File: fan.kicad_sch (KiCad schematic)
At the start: 15 parts, among them J5001 Conn_01x04, U5001 EMC2103-2

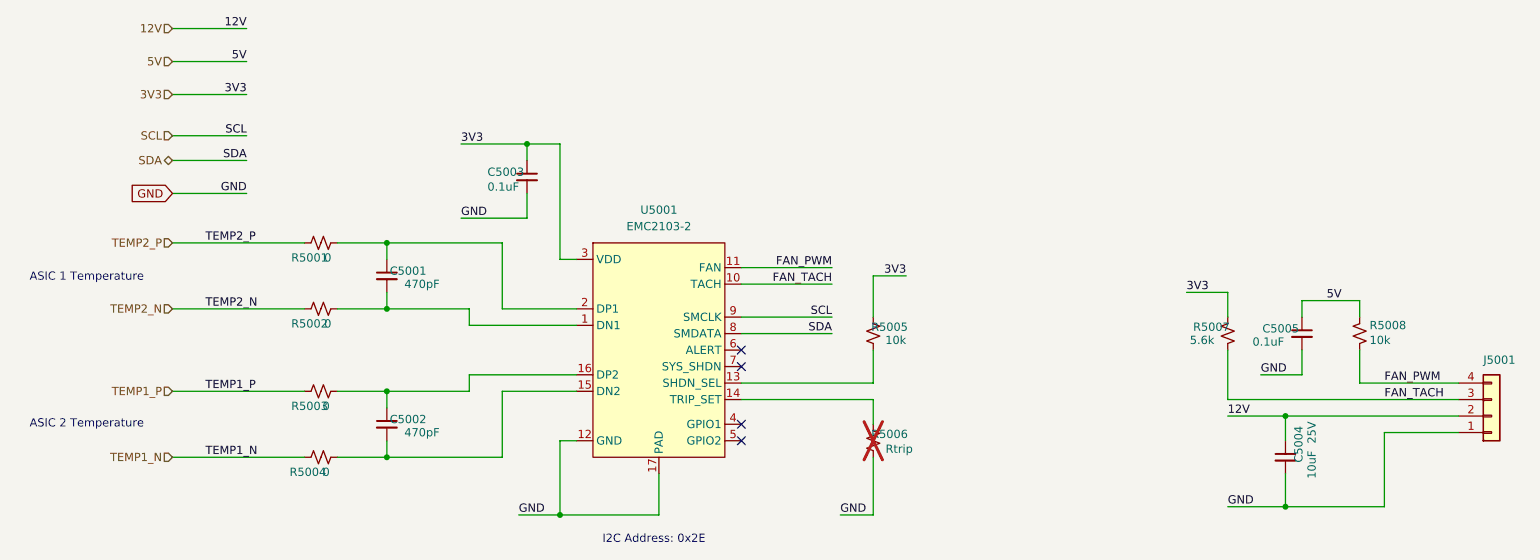
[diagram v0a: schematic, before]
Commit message: finished adding ASICs to schematic. Change VR to single phase 2.8V output
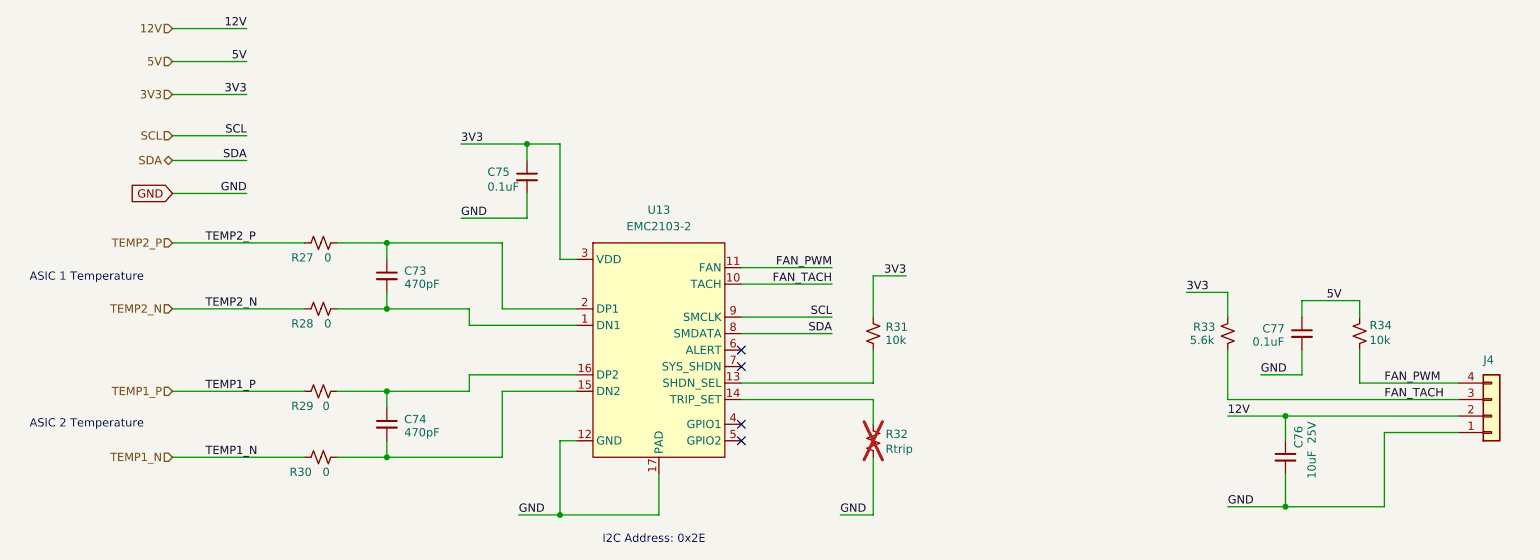
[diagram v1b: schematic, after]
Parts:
- renumbered C5001 to C73, C5002 to C74, C5003 to C75, C5004 to C76, C5005 to C77, J5001 to J4, R5001 to R27, R5002 to R28, R5003 to R29, R5004 to R30, R5005 to R31, R5006 to R32, R5007 to R33, R5008 to R34, U5001 to U13
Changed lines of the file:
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@@
 		(on_board yes)
 		(dnp no)
-		(property "Reference" "R5003"
+		(property "Reference" "R29"
 			(at 75.438 105.156 90)
 			(effects
@@
 			(project "BitaxeGT"
 				(path "/61fe8d2c-9301-4ad9-8caf-c47acfa835b0/edab3562-ad75-4c4e-afab-a1841dcf5714"
-					(reference "R5003")
+					(reference "R29")
 					(unit 1)
 				)
@@
 		(on_board yes)
 		(dnp yes)
-		(property "Reference" "R5006"
+		(property "Reference" "R32"
 			(at 170.434 109.474 0)
 			(effects
@@
 			(project "BitaxeGT"
 				(path "/61fe8d2c-9301-4ad9-8caf-c47acfa835b0/edab3562-ad75-4c4e-afab-a1841dcf5714"
-					(reference "R5006")
+					(reference "R32")
 					(unit 1)
 				)
@@
 		(dnp no)
 		(fields_autoplaced yes)
-		(property "Reference" "U5001"
+		(property "Reference" "U13"
 			(at 132.08 74.93 0)
 			(effects
@@
 			(project ""
 				(path "/61fe8d2c-9301-4ad9-8caf-c47acfa835b0/edab3562-ad75-4c4e-afab-a1841dcf5714"
-					(reference "U5001")
+					(reference "U13")
 					(unit 1)
 				)
@@
 		(on_board yes)
 		(dnp no)
-		(property "Reference" "C5001"
+		(property "Reference" "C73"
 			(at 96.266 84.328 0)
 			(effects
@@
 			(project "BitaxeGT"
 				(path "/61fe8d2c-9301-4ad9-8caf-c47acfa835b0/edab3562-ad75-4c4e-afab-a1841dcf5714"
-					(reference "C5001")
+					(reference "C73")
 					(unit 1)
 				)
@@
 		(on_board yes)
 		(dnp no)
-		(property "Reference" "R5005"
+		(property "Reference" "R31"
 			(at 170.434 92.964 0)
 			(effects
@@
 			(project "BitaxeGT"
 				(path "/61fe8d2c-9301-4ad9-8caf-c47acfa835b0/edab3562-ad75-4c4e-afab-a1841dcf5714"
-					(reference "R5005")
+					(reference "R31")
 					(unit 1)
 				)
@@
 		(on_board yes)
 		(dnp no)
-		(property "Reference" "R5008"
+		(property "Reference" "R34"
 			(at 241.554 92.71 0)
 			(effects
@@
 			(project "BitaxeGT"
 				(path "/61fe8d2c-9301-4ad9-8caf-c47acfa835b0/edab3562-ad75-4c4e-afab-a1841dcf5714"
-					(reference "R5008")
+					(reference "R34")
 					(unit 1)
 				)
@@
 		(on_board yes)
 		(dnp no)
-		(property "Reference" "C5002"
+		(property "Reference" "C74"
 			(at 96.266 107.188 0)
 			(effects
@@
 			(project "BitaxeGT"
 				(path "/61fe8d2c-9301-4ad9-8caf-c47acfa835b0/edab3562-ad75-4c4e-afab-a1841dcf5714"
-					(reference "C5002")
+					(reference "C74")
 					(unit 1)
 				)
@@
 		(on_board yes)
 		(dnp no)
-		(property "Reference" "J5001"
+		(property "Reference" "J4"
 			(at 259.08 98.044 0)
 			(effects
@@
 			(project "BitaxeGT"
 				(path "/61fe8d2c-9301-4ad9-8caf-c47acfa835b0/edab3562-ad75-4c4e-afab-a1841dcf5714"
-					(reference "J5001")
+					(reference "J4")
 					(unit 1)
 				)
@@
 		(on_board yes)
 		(dnp no)
-		(property "Reference" "R5004"
+		(property "Reference" "R30"
 			(at 75.184 115.316 90)
 			(effects
@@
 			(project "BitaxeGT"
 				(path "/61fe8d2c-9301-4ad9-8caf-c47acfa835b0/edab3562-ad75-4c4e-afab-a1841dcf5714"
-					(reference "R5004")
+					(reference "R30")
 					(unit 1)
 				)
@@
 		(on_board yes)
 		(dnp no)
-		(property "Reference" "R5007"
+		(property "Reference" "R33"
 			(at 214.376 92.964 0)
 			(effects
@@
 			(project "BitaxeGT"
 				(path "/61fe8d2c-9301-4ad9-8caf-c47acfa835b0/edab3562-ad75-4c4e-afab-a1841dcf5714"
-					(reference "R5007")
+					(reference "R33")
 					(unit 1)
 				)
@@
 		(on_board yes)
 		(dnp no)
-		(property "Reference" "C5003"
+		(property "Reference" "C75"
 			(at 105.664 69.088 0)
 			(effects
@@
 			(project "BitaxeGT"
 				(path "/61fe8d2c-9301-4ad9-8caf-c47acfa835b0/edab3562-ad75-4c4e-afab-a1841dcf5714"
-					(reference "C5003")
+					(reference "C75")
 					(unit 1)
 				)
@@
 		(on_board yes)
 		(dnp no)
-		(property "Reference" "C5005"
+		(property "Reference" "C77"
 			(at 225.044 93.218 0)
 			(effects
@@
 			(project "BitaxeGT"
 				(path "/61fe8d2c-9301-4ad9-8caf-c47acfa835b0/edab3562-ad75-4c4e-afab-a1841dcf5714"
-					(reference "C5005")
+					(reference "C77")
 					(unit 1)
 				)
@@
 		(on_board yes)
 		(dnp no)
-		(property "Reference" "R5002"
+		(property "Reference" "R28"
 			(at 75.438 92.456 90)
 			(effects
@@
 			(project "BitaxeGT"
 				(path "/61fe8d2c-9301-4ad9-8caf-c47acfa835b0/edab3562-ad75-4c4e-afab-a1841dcf5714"
-					(reference "R5002")
+					(reference "R28")
 					(unit 1)
 				)
@@
 		(on_board yes)
 		(dnp no)
-		(property "Reference" "C5004"
+		(property "Reference" "C76"
 			(at 230.632 108.204 90)
 			(effects
@@
 			(project "BitaxeGT"
 				(path "/61fe8d2c-9301-4ad9-8caf-c47acfa835b0/edab3562-ad75-4c4e-afab-a1841dcf5714"
-					(reference "C5004")
+					(reference "C76")
 					(unit 1)
 				)
@@
 		(on_board yes)
 		(dnp no)
-		(property "Reference" "R5001"
+		(property "Reference" "R27"
 			(at 75.438 82.296 90)
 			(effects
@@
 			(project "BitaxeGT"
 				(path "/61fe8d2c-9301-4ad9-8caf-c47acfa835b0/edab3562-ad75-4c4e-afab-a1841dcf5714"
-					(reference "R5001")
-					(unit 1)
-				)
+					(reference "R27")
+					(unit 1)
+				)

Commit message: Removed EMC2103, added discrete fan control, DRC pass, fixed logo.
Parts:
- removed C73, C74: 470pF, Capacitor_SMD:C_0402_1005Metric, symbol Device:C_Small
- removed C75: 0.1uF, Capacitor_SMD:C_0402_1005Metric, symbol Device:C_Small
- removed R27, R28, R29, R30: 0, Resistor_SMD:R_0402_1005Metric, symbol Device:R_Small_US
- removed R31: 10k, Resistor_SMD:R_0402_1005Metric, symbol Device:R_Small_US
- removed R32: Rtrip, Resistor_SMD:R_0402_1005Metric, symbol Device:R_Small_US
- removed U13: EMC2103-2, Package_DFN_QFN:QFN-16-1EP_4x4mm_P0.65mm_EP2.1x2.1mm, symbol bitaxe:EMC2103-2
- added D13: 3.3V Zener, Diode_SMD:D_SOD-123, symbol Device:D_Zener_Small_Filled
- added Q1: BSS138, Package_TO_SOT_SMD:SOT-23, symbol Transistor_FET:BSS138
- added R1: 1k, Resistor_SMD:R_0402_1005Metric, symbol Device:R_Small_US
- added R2: 10k, Resistor_SMD:R_0402_1005Metric, symbol Device:R_Small_US
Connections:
- net FAN_PWM: now also R1.2; no longer J4.4 (Pin_4), R34.1
- net FAN_TACH: now also R2.2; no longer J4.3 (Pin_3), R33.1
- net GND: now also D13.2 (A), Q1.2 (S)
- new net: Q1.1 (G), R1.1
- new net FAN_PWM_PIN: J4.4 (Pin_4), Q1.3 (D), R34.1
- new net FAN_TACH_PIN: D13.1 (K), J4.3 (Pin_3), R2.1, R33.1
- no-connect marks 4 -> 0
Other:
- note removed: "ASIC 1 Temperature"
- note removed: "ASIC 2 Temperature"
- note removed: "I2C Address: 0x2E"
- moved on the sheet: C76, C77, J4, R33, R34

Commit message: power plane cleanup. added field vias. generated BOM
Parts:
- R1: DK (none) -> 311-1.00KLRCT-ND; PARTNO (none) -> RC0402FR-071KL
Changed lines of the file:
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@@
 		(title "Bitaxe Intel Reference Design System")
 		(date "2025-10-01")
-		(rev "1300x")
+		(rev "1300xx")
 	)
 	(junction
@@
 			)
 		)
+		(property "Manufacturer" ""
+			(at 127 92.71 0)
+			(effects
+				(font
+					(size 1.27 1.27)
+				)
+				(hide yes)
+			)
+		)
 		(pin "3"
 		)
@@
 			)
 		)
+		(property "Manufacturer" ""
+			(at 168.91 91.44 90)
+			(effects
+				(font
+					(size 1.27 1.27)
+				)
+				(hide yes)
+			)
+		)
 		(pin "2"
 		)
@@
 			)
 		)
+		(property "Manufacturer" ""
+			(at 229.87 80.01 0)
+			(effects
+				(font
+					(size 1.27 1.27)
+				)
+				(hide yes)
+			)
+		)
 		(pin "2"
 		)
@@
 			)
 		)
+		(property "Manufacturer" ""
+			(at 175.26 99.06 90)
+			(effects
+				(font
+					(size 1.27 1.27)
+				)
+				(hide yes)
+			)
+		)
 		(pin "1"
 		)
@@
 			)
 		)
+		(property "Manufacturer" ""
+			(at 250.19 92.71 0)
+			(effects
+				(font
+					(size 1.27 1.27)
+				)
+				(hide yes)
+			)
+		)
 		(pin "4"
 		)
@@
 			)
 		)
+		(property "Manufacturer" ""
+			(at 209.55 80.01 0)
+			(effects
+				(font
+					(size 1.27 1.27)
+				)
+				(hide yes)
+			)
+		)
 		(pin "2"
 		)
@@
 			)
 		)
-		(property "PARTNO" ""
+		(property "PARTNO" "RC0402FR-071KL"
 			(at 111.76 92.71 0)
 			(effects
@@
 			)
 		)
-		(property "DK" ""
+		(property "DK" "311-1.00KLRCT-ND"
 			(at 111.76 92.71 0)
 			(effects
@@
 		(property "Mouser" ""
 			(at 111.76 92.71 0)
+			(effects
+				(font
+					(size 1.27 1.27)
+				)
+				(hide yes)
+			)
+		)
+		(property "Manufacturer" ""
+			(at 111.76 92.71 90)
 			(effects
 				(font
@@
 			)
 		)
+		(property "Manufacturer" ""
+			(at 220.98 80.01 0)
+			(effects
+				(font
+					(size 1.27 1.27)
+				)
+				(hide yes)
+			)
+		)
 		(pin "1"
 		)
@@
 			(at 218.44 99.06 90)
 			(effects
+				(font
+					(size 1.27 1.27)
+				)
+				(hide yes)
+			)
+		)
+		(property "Manufacturer" ""
+			(at 218.44 99.06 90)
+			(effects
